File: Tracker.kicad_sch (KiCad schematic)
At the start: 10 parts, among them J1 Conn_01x04_Pin, J2 Conn_01x04, Q1 Q_NMOS_GSD, U1 LOC112P, U2 LM74700

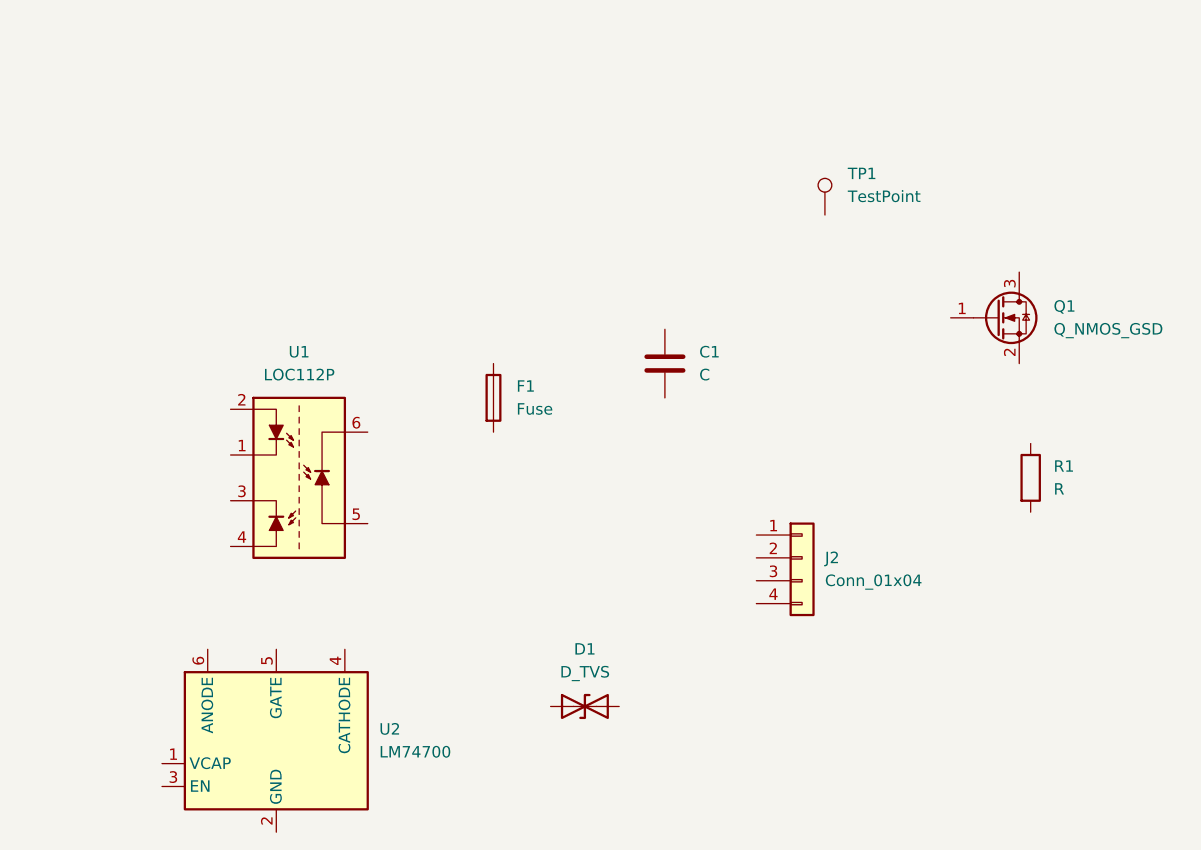
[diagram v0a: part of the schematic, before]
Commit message: Add BG95 modem sheet to Tracker
Added a new root schematic sheet for the Quectel BG95-M3 cellular module and the SIM card connector. Updated the KiCad project metadata to include the new sheet and register the associated power net and symbol references so the design is fully linked in the project.
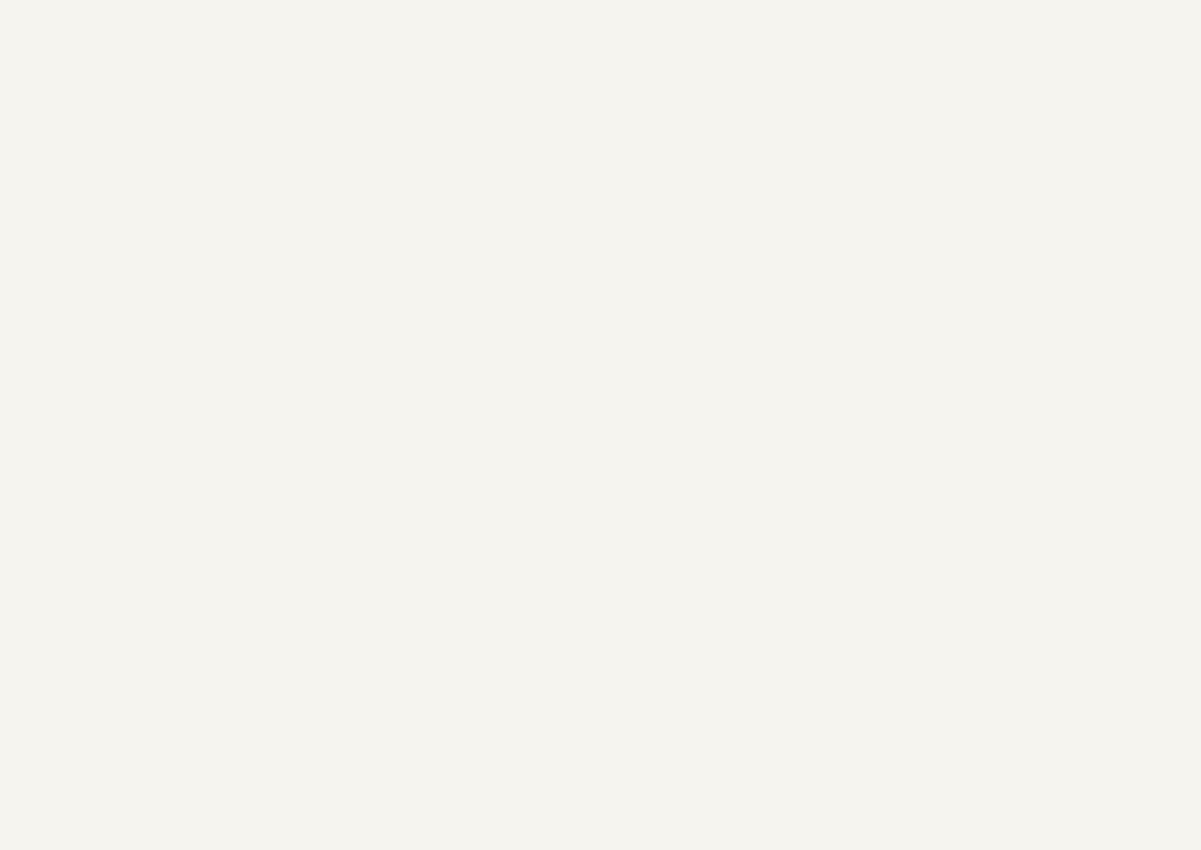
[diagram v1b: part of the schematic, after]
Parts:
- removed C1: C, symbol Device:C
- removed D1: D_TVS, symbol Device:D_TVS
- removed F1: Fuse, Package_QFP:PQFP-160_28x28mm_P0.65mm, symbol Device:Fuse
- removed J2: Conn_01x04, Package_TO_SOT_SMD:SOT-23-6, symbol Connector_Generic:Conn_01x04
- removed Q1: Q_NMOS_GSD, Package_QFP:TQFP-44_10x10mm_P0.8mm, symbol Transistor_FET:Q_NMOS_GSD
- removed R1: R, symbol Device:R
- removed TP1: TestPoint, Package_QFP:TQFP-44_10x10mm_P0.8mm, symbol Connector:TestPoint
- removed U1: LOC112P, Package_DIP:IXYS_Flatpak-8_6.3x9.7mm_P2.54mm, symbol Isolator_Analog:LOC112P
- removed U2: LM74700, Package_TO_SOT_SMD:SOT-23-6, symbol Power_Management:LM74700

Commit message: Update BG95 schematic and power nets
This commit revises the tracker schematic to match the updated BG95 and power-distribution design. It adds missing power flags and net labels, updates component references and footprints, adds coaxial and connector symbols, and swaps several passives/ferrite beads to better reflect the final BOM. The netlist is also cleaned up by renaming references and correcting no-connect/power pin assignments so the KiCad project remains consistent and ERC-friendly.
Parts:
- removed J1: Conn_01x04_Pin, Package_DIP:IXYS_Flatpak-8_6.3x9.7mm_P2.54mm, symbol Connector:Conn_01x04_Pin
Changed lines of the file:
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@@
 	(generator_version "10.0")
 	(paper "A1")
-	(symbol
-		(lib_id "Connector:Conn_01x04_Pin")
-		(at -1282.7 -607.06 0)
-		(unit 1)
-		(body_style 1)
-		(exclude_from_sim no)
-		(in_bom yes)
-		(on_board yes)
-		(in_pos_files yes)
-		(dnp no)
-		(fields_autoplaced yes)
-		(property "Reference" "J1"
-			(at -1282.065 -613.41 0)
-			(show_name no)
-			(do_not_autoplace no)
-			(effects
-				(font
-					(size 1.27 1.27)
-				)
-			)
-		)
-		(property "Value" "Conn_01x04_Pin"
-			(at -1282.065 -610.87 0)
-			(show_name no)
-			(do_not_autoplace no)
-			(effects
-				(font
-					(size 1.27 1.27)
-				)
-			)
-		)
-		(property "Footprint" "Package_DIP:IXYS_Flatpak-8_6.3x9.7mm_P2.54mm"
-			(at -1282.7 -607.06 0)
-			(hide yes)
-			(show_name no)
-			(do_not_autoplace no)
-			(effects
-				(font
-					(size 1.27 1.27)
-				)
-			)
-		)
-		(property "Datasheet" ""
-			(at -1282.7 -607.06 0)
-			(hide yes)
-			(show_name no)
-			(do_not_autoplace no)
-			(effects
-				(font
-					(size 1.27 1.27)
-				)
-			)
-		)
-		(property "Description" "Generic connector, single row, 01x04, script generated"
-			(at -1282.7 -607.06 0)
-			(hide yes)
-			(show_name no)
-			(do_not_autoplace no)
-			(effects
-				(font
-					(size 1.27 1.27)
-				)
-			)
-		)
-		(pin "4"
-		)
-		(pin "3"
-		)
-		(pin "1"
-		)
-		(pin "2"
-		)
-		(instances
-			(project "Tracker"
-				(path "/586d1ea1-b017-4713-987c-545d658f6cc8"
-					(reference "J1")
-					(unit 1)
-				)
-			)
-		)
-	)
 	(sheet_instances
 		(path "/"

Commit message: Add GNSS and power protection
This update expands the Tracker schematic with vehicle input protection, GNSS receiver connectivity, and additional power/measurement components. It also refreshes KiCad symbol metadata and designator assignments, and renames the page-2 connector reference from J2 to J901 to match the updated schematic and BOM.
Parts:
- added C1, C3, C4: 22nF 100V, Package_SO:SOIC-8_3.9x4.9mm_P1.27mm, symbol Device:C
- added C2: C, Package_SO:SOIC-8_3.9x4.9mm_P1.27mm, symbol Device:C
- added C2: 100nF 25V, Package_SO:SOIC-8_3.9x4.9mm_P1.27mm, symbol Device:C
- added C321: 10uF, Package_SO:SOIC-8_3.9x4.9mm_P1.27mm, symbol Device:C
- added C322: 100uF, Package_SO:SOIC-8_3.9x4.9mm_P1.27mm, symbol Device:C
- added C323: 100nF, Package_SO:SOIC-8_3.9x4.9mm_P1.27mm, symbol Device:C
- added C5: 10nF, Package_SO:SOIC-8_3.9x4.9mm_P1.27mm, symbol Device:C
- added D3: SMBJ33CA, DIONM5436X244N, symbol SamacSys_Parts:SMBJ33CA
- added F1: Fuse, symbol Device:Fuse
- added IC1, IC2: BQ25601DRTWR, QFN50P400X400X80-25N-D, symbol SamacSys_Parts:BQ25601DRTWR
- added J1: Vehicle 12V 2X2, Package_TO_SOT_SMD:SOT-23, symbol Project_Parts:Vehicle 12V 2X2
- added J303: Conn_Coaxial, Package_DFN_QFN:WDFN-10-1EP_3x3mm_P0.5mm_EP1.8x2.5mm, symbol Connector:Conn_Coaxial
- added L301: 27nH, Relay_THT:Relay_DPDT_Finder_30.22, symbol Device:L
- added Q2, Q4: 2N7002, Package_TO_SOT_SMD:SOT-23, symbol Transistor_FET:2N7002
- added Q3: DMT6007LFGQ-7, DMTH8008LFGQ7, symbol SamacSys_Parts:DMT6007LFGQ-7
- added R3: 100k, symbol Device:R
- added R313, R314, R316, R317, R318: 10R, symbol Device:R
- added R4: 22k, symbol Device:R
- added TP1: TP 1, DMTH8008LFGQ7, symbol Connector:TestPoint
- added TP309: TP 309, RF_GPS:ublox_MAX, symbol Connector:TestPoint
- added TP310: TP 310, RF_GPS:ublox_MAX, symbol Connector:TestPoint
- added TP311: TP 311, RF_GPS:ublox_MAX, symbol Connector:TestPoint
- added U1: LM74700, Package_TO_SOT_SMD:SOT-23-6, symbol Power_Management:LM74700
- added U305: MAX-M10S, RF_GPS:ublox_MAX, symbol RF_GPS:MAX-M10S
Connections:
- new net: C5.1, Q2.1 (G), R3.1, R4.2
- new net: C1.1, C2.1, D3.2, F1.2, Q3.1 (S_1), Q3.2 (S_2), Q3.3 (S_3), U1.3 (EN), U1.6 (ANODE)
- new net: Q3.4 (G), U1.5 (GATE)
- new net: TP311.1, U305.18 (~{SAFEBOOT})
- new net: C2.2, U1.1 (VCAP)
- new net: J303.1 (In), L301.1, U305.14 (VCC_RF)
- new net: L301.2, R313.2
- new net: F1.1, J1.1 (Batery_12V)
- new net: R313.1, U305.11 (RF_IN)
- new net: TP309.1, U305.4 (TIMEPULSE)
- new net: TP310.1, U305.9 (~{RESET})
- new net 3V3_AON: C323.1, R316.2, U305.6 (V_BCKP)
- new net 3V3_AUX: C321.1, C322.1, U305.7 (VCC_IO), U305.8 (VCC)
- new net GND: C1.2, C3.2, C321.2, C322.2, C323.2, C4.2, C5.2, D3.1, J1.2 (GND), J303.2 (Ext), Q2.2 (S), R314.1, R317.1, R4.1, U1.2 (GND), U305.1 (GND), U305.10 (GND), U305.12 (GND)
- new net GNSS_UART_RX: U305.2 (TXD)
- new net GNSS_UART_TX: U305.3 (RXD)
- new net IGN_IN: J1.3 (Ignition), R3.2
- new net IGN_WAKE_N: Q2.3 (D), R316.1
- new net VIN_PROT: C3.1, Q3.5 (D_1), R318.2, TP1.1, U1.4 (CATHODE)
- new net VIN_SENSE: C4.1, R317.2, R318.1
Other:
- note added: "GNSS RECEIVER"
- note added: "VEHICLE INPUT"

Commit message: More adjustment
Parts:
- removed C2: C, Package_SO:SOIC-8_3.9x4.9mm_P1.27mm, symbol Device:C
- removed IC2: BQ25601DRTWR, QFN50P400X400X80-25N-D, symbol SamacSys_Parts:BQ25601DRTWR
- removed R314: 10R, symbol Device:R
- added C10, C11: 47uF 100V, Package_SO:SOIC-8_3.9x4.9mm_P1.27mm, symbol Device:C
- added C12: 470nF 16V, Package_SO:SOIC-8_3.9x4.9mm_P1.27mm, symbol Device:C
- added C13: 2.2uF 10V, Package_SO:SOIC-8_3.9x4.9mm_P1.27mm, symbol Device:C
- added C14: 1uF 10V, Package_SO:SOIC-8_3.9x4.9mm_P1.27mm, symbol Device:C
- added C15: 120pF C0G, Package_SO:SOIC-8_3.9x4.9mm_P1.27mm, symbol Device:C
- added C16, C17, C18: 47uF 10V, Package_SO:SOIC-8_3.9x4.9mm_P1.27mm, symbol Device:C
- added C23: 1uF 25V, Package_SO:SOIC-8_3.9x4.9mm_P1.27mm, symbol Device:C
- added C24: 10uF 25V, Package_SO:SOIC-8_3.9x4.9mm_P1.27mm, symbol Device:C
- added C26, C28, C30, C32: 10uF 10V, Package_SO:SOIC-8_3.9x4.9mm_P1.27mm, symbol Device:C
- added C29: 4.7uF 10V, Package_SO:SOIC-8_3.9x4.9mm_P1.27mm, symbol Device:C
- added C6, C7: 2.2uF 100V, Package_SO:SOIC-8_3.9x4.9mm_P1.27mm, symbol Device:C
- added C8, C9: 4.7uF 100V, Package_SO:SOIC-8_3.9x4.9mm_P1.27mm, symbol Device:C
- added D2: LED green, QFN50P400X400X80-25N-D, symbol Device:LED
- added L1: 1uH Isat >=4A, Relay_THT:Relay_DPDT_Finder_30.22, symbol Device:L
- added L3: 1uH Isat >=3.5A, Relay_THT:Relay_DPDT_Finder_30.22, symbol Device:L
- added R10: 402k 1%, symbol Device:R
- added R11, R7, R8: 100k 1%, symbol Device:R
- added R23: 30.9k 1%, symbol Device:R
- added R26, R27: 100k, symbol Device:R
- added R28: 20m 1% 1W, symbol Device:R
- added R321, R322, R323: 10R, symbol Device:R
- added R6: 4.7R, symbol Device:R
- added R9: 24.9k 1%, symbol Device:R
- added TH1: 10k NTC, Resistor_THT:R_Array_SIP4, symbol Device:Thermistor_NTC
- added TP4: (no value), Relay_THT:Relay_DPDT_Schrack-RT2-FormC_RM5mm, symbol Connector:TestPoint
- added TP5: TP 5, Relay_THT:Relay_DPDT_Schrack-RT2-FormC_RM5mm, symbol Connector:TestPoint
- added TP6: TP 6, Relay_THT:Relay_DPDT_Schrack-RT2-FormC_RM5mm, symbol Connector:TestPoint
- added U2: LM76003QRNPRQ1, LM76003QRNPRQ1, symbol SamacSys_Parts:LM76003QRNPRQ1
- renumbered IC1 to U5
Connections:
- net GND: now also Q4.2 (S), U5.17 (GND_1), U5.18 (GND_2), U5.25 (EP), C10.1, C11.1, C13.1, C14.2, C16.1, C17.1, C18.1, C23.2, C24.1, C26.2, C28.2, C29.2, C32.2, C6.1, C7.1, C8.1, C9.1, R11.1, R23.1, R27.1, R7.1, R9.1, TH1.2, U2.13 (AGND_1), U2.14 (AGND_2), U2.15 (AGND_3), U2.17 (SYNC/MODE), U2.19 (NC_2), U2.23 (NC_3), U2.24 (PGND_1), U2.25 (PGND_2), U2.26 (PGND_3), U2.27 (NC_4), U2.28 (NC_5), U2.29 (NC_6), U2.30 (NC_7), U2.31 (EP), U2.7 (NC_1)
- net VIN_PROT: now also C6.2, C7.2, L1.1
- net VBUS_CHG: now reaches U5.1 (VBUS)
- net VBUS_CHG: now also U5.24 (VAC), C23.1
- net at U5.11 (TS): now also R23.2, R321.2, TH1.1
- net at U5.12 (~{QON}): now also TP4.1
- net BAT_CHG: now reaches U5.13 (BAT_1)
- net BAT_CHG: now also U5.14 (BAT_2), C28.1, R323.2
- net SYS_CHG: now reaches U5.15 (SYS_1)
- net SYS_CHG: now also U5.16 (SYS_2), C26.1, C32.1, L3.2, R28.2
- net at U5.19 (SW_1): now also U5.20 (SW_2), C30.1, L3.1
- net at U5.21 (BTST): now also C30.2
- net REGN: now reaches U5.22 (REGN)
- net REGN: now also Q4.3 (D), C29.1, R26.2, R321.1, R322.1
- net at U5.23 (PMID): now also C24.2
- net at U5.4 (STAT): now also D2.1 (K)
- net I2C_SCL: now reaches U5.5 (SCL)
- net I2C_SDA: now reaches U5.6 (SDA)
- net CHG_INT_N: now reaches U5.7 (~{INT})
- net at U5.9 (~{CE}): now also R26.1
- net CHG_EN: now reaches Q4.1 (G)
- net CHG_EN: now also R27.2
- new net: C14.1, R6.2, U2.9 (BIAS)
- new net: D2.2 (A), R322.2
- new net: C15.1, R8.2, R9.2, U2.12 (FB)
- new net: R7.2, U2.10 (RT)
- new net: R10.1, R11.2, U2.18 (EN)
- new net: C10.2, C11.2, C8.2, C9.2, L1.2, R10.2, U2.20 (PVIN_1), U2.21 (PVIN_2), U2.22 (PVIN_3)
- new net: C12.1, U2.6 (BOOT)
- new net: C13.2, U2.8 (VCC)
- new net 5V_VEH: C12.2, C15.2, C16.2, C17.2, C18.2, R6.1, R8.1, U2.1 (SW_1), U2.2 (SW_2), U2.3 (SW_3), U2.4 (SW_4), U2.5 (SW_5)
- new net BAT_CELL: R323.1, TP6.1
- new net BUCK_PG: U2.16 (PGOOD)
- new net VSYS: R28.1, TP5.1
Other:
- note added: "CHARGER + POWER PATH"
- moved on the sheet: Q4

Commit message: 5V source MUX
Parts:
- added C19: 100nF, symbol Device:C
- added C20, C21: 1uF 16V, symbol Device:C
- added C22: 4.7uF 16V, symbol Device:C
- added R13: 316k 1%, TPS2121RUXR, symbol Device:R
- added R14: 100k 1%, TPS2121RUXR, symbol Device:R
- added R15: 237% 1%, TPS2121RUXR, symbol Device:R
- added R16, R18: 49.9k 1%, TPS2121RUXR, symbol Device:R
- added R17: 237k 1%, TPS2121RUXR, symbol Device:R
- added R19: 30.1k 1%, TPS2121RUXR, symbol Device:R
- added R21: 20m 1% 1W, TPS2121RUXR, symbol Device:R
- added TP3: TestPoint, symbol Connector:TestPoint
- added U3: TPS2121RUXR, TPS2121RUXR, symbol SamacSys_Parts:TPS2121RUXR
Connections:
- net GND: now also C19.2, C20.2, C21.2, C22.2, R14.2, R16.2, R18.2, R19.1, U3.12 (GND), U3.3 (CP2)
- net VBUS_CHG: now also R21.2
- new net: R13.2, R14.1, U3.6 (PR1)
- new net: C22.1, R21.1, TP3.1, U3.1 (OUT_1), U3.8 (OUT_2)
- new net: R15.2, R16.1, U3.5 (OV1)
- new net: C19.1, U3.11 (SS)
- new net: R17.2, R18.1, U3.4 (OV2)
- new net: R19.2, U3.10 (ILIM)
- new net MUX_ST: U3.9 (ST)
- new net VBUS_USB: C21.1, R17.1, U3.2 (IN2)
- new net VCC: C20.1, R13.1, R15.1, U3.7 (IN1)
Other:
- note added: "5V SOURCE MUX"
- note added: "INPUT FILTER + AUTOMOTIVE BUCK"

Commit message: power
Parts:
- added BT1: BHC-18650-1P, BHC186501P, symbol SamacSys_Parts:BHC-18650-1P
- added C30, C31, C32: 100nF, QFN65P400X400X100-17N-D, symbol Device:C
- added Q1, Q5: CSD16406Q3, DQG_VSON-CLIP, symbol SamacSys_Parts:CSD16406Q3
- added R31: 2.2k, symbol Device:R
- added R32, R33: 5.2M, symbol Device:R
- added TP12: TP 12, symbol Connector:TestPoint
- added TP13: TP 13, symbol Connector:TestPoint
- added U4: INA3221AIRGVR, QFN65P400X400X100-17N-D, symbol SamacSys_Parts:INA3221AIRGVR
- added U6: BQ29700DSER, SON50P150X150X80-6N, symbol SamacSys_Parts:BQ29700DSER
- added U7: TPS3840DL35DBVR, SOT95P280X145-5N, symbol SamacSys_Parts:TPS3840DL35DBVR
- C25: renamed from C30; value 10uF 10V -> 47Nf 16v
- renumbered C32 to C27
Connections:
- net 3V3_AON: now also C30.1, U4.16 (VPU), U4.4 (VS)
- net BAT_CELL: now also BT1.1 (-), C31.1, U4.1 (IN-3), U6.5 (BAT)
- net BAT_CHG: now also U4.2 (IN+3)
- net GND: now also C30.2, C32.2, Q5.1 (S_1), Q5.2 (S_2), Q5.3 (S_3), R31.1, R33.2, TP12.1, TP13.1, U4.17 (GND_2), U4.3 (GND_1), U4.5 (A0), U7.3 (GND)
- net I2C_SDA: now also U4.7 (SDA)
- net SYS_CHG: now also U4.15 (IN+2)
- net VBUS_CHG: now also U4.11 (IN-1)
- net VSYS: now also C32.1, U4.14 (IN-2), U7.2 (VDD), U7.4 (~{MR}/NC)
- new net: Q5.4 (G), R33.1, U6.3 (DOUT)
- new net: BT1.2 (+), C31.2, Q1.1 (S_1), Q1.2 (S_2), Q1.3 (S_3), R32.2, U6.4 (VSS)
- new net: Q1.4 (G), R32.1, U6.2 (COUT)
- new net: R31.2, U6.6 (V-)
- new net: Q1.5 (D_1), Q5.5 (D_1)
- new net ICC_SCL: U4.6 (SCL)
- new net PM_ALERT_N: U4.8 (WARNING), U4.9 (CRITICAL)
- new net SYS_LOW_N: U7.1 (~{RESET})
- new net VBUS_MUX: U4.12 (IN+1)
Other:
- note added: "BACKUP CELL"
- note added: "POWER MONITORING"

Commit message: dec
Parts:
- removed TP12: TP 12, symbol Connector:TestPoint
- removed TP13: TP 13, symbol Connector:TestPoint
- added C33, C37, C38, C46, C47: 10uF 10V, QFN65P400X400X100-17N-D, symbol Device:C
- added C34, C35, C39, C40, C41: 22uF 10V, QFN65P400X400X100-17N-D, symbol Device:C
- added C36: 220uF 6.3V polymer, QFN65P400X400X100-17N-D, symbol Device:C_Polarized
- added C42: 100nF, QFN65P400X400X100-17N-D, symbol Device:C
- added C43, C45: 4.7uF 10V, QFN65P400X400X100-17N-D, symbol Device:C
- added CSC1: 1F 2.7V, QFN65P400X400X100-17N-D, symbol Device:C_Polarized
- added L4: 0.47uH 5.4A, Relay_THT:Relay_DPDT_Finder_30.22, symbol Device:L
- added L5: 2.2uH 4.4A, Relay_THT:Relay_DPDT_Finder_30.22, symbol Device:L
- added L7, L8: 2.2uH, Relay_THT:Relay_DPDT_Finder_30.22, symbol Device:L
- added R29: 6.65k 1%, symbol Device:R
- added R35, R36: R, TPS2121RUXR, symbol Device:R
- added R37: 100k, TPS2121RUXR, symbol Device:R
- added R39: 4.75k 1%, symbol Device:R
- added R40: 22.1k 1%, symbol Device:R
- added R42, R43: 1M 1%, symbol Device:R
- added R44, R45: 267k 1%, symbol Device:R
- added R46: 100k, symbol Device:R
- added TP10, TP11, TP9: TP 9, symbol Connector:TestPoint
- added TP208: TP 208, symbol Connector:TestPoint
- added U10, U11: TPS62840DLCR, SON50P150X200X100-8N-D, symbol SamacSys_Parts:TPS62840DLCR
- added U8: TPS63802DLAR, TPS63802DLAR, symbol SamacSys_Parts:TPS63802DLAR
- added U9: TPS61094DSSR, SON50P200X300X80-13N-D, symbol SamacSys_Parts:TPS61094DSSR
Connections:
- net ICC_SCL is gone; now on net I2C_SCL: U4.6 (SCL)
- net 3V3_AON: now also C47.1, L8.2, TP10.1, U10.7 (SW)
- net 3V3_AUX: now also C46.1, L7.2, TP11.1, U11.8 (VOS)
- net GND: now also C33.2, C34.2, C35.2, C36.2, C37.2, C38.2, C39.2, C40.2, C41.2, C42.2, C43.2, C45.2, C46.2, C47.2, CSC1.2, R29.1, R36.2, R37.2, R39.1, R40.1, R43.1, R44.2, R45.2, R46.2, U10.1 (GND), U10.3 (MODE), U10.6 (STOP), U11.1 (GND), U11.3 (MODE), U11.6 (STOP), U8.2 (MODE), U8.3 (AGND), U8.8 (GND), U9.13 (EP), U9.7 (PGND), U9.8 (AGND)
- net VBAT_BG95: now also C34.1, C35.1, C36.1, R35.1, U8.6 (VOUT)
- net VSYS: now also C33.1, C37.1, C45.1, U11.2 (VIN), U8.10 (VIN), U9.2 (MODE), U9.3 (EN), U9.4 (VIN)
- new net: R44.1, U10.5 (VSET)
- new net: L8.1, U10.8 (VOS)
- new net: R45.1, U11.5 (VSET)
- new net: L7.1, U11.7 (SW)
- new net: R29.2, U9.12 (VCHG)
- new net: L4.1, U8.9 (L1)
- new net: L4.2, U8.7 (L2)
- new net: L5.1, U9.5 (SW)
- new net: C38.1, CSC1.1, L5.2, R42.2, U9.6 (SUP)
- new net: R39.2, U9.1 (OSEL)
- new net: R40.2, U9.11 (ICHG)
- new net: TP208.1, U8.5 (PG)
- new net: R35.2, R36.1, U8.4 (FB)
- new net AUX_EN: R46.1, U11.4 (EN)
- new net BG95_PWR_EN: R37.1, U8.1 (EN)
- new net VOUT_SC: C39.1, C40.1, C41.1, C43.1, TP9.1, U10.2 (VIN), U10.4 (EN), U9.10 (VOUT_2), U9.9 (VOUT_1)
- new net VSUP_SENSE: C42.1, R42.1, R43.2
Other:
- note added: "3.3V RAIL"
- note added: "BG95-M3 SUPPLY"
- note added: "LAST-GASP"
- moved on the sheet: BT1, C1, C10, C11, C12, C13, C14, C15, C16, C17, C18, C19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

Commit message: hierarchy
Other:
- added sheet CELLULAR (cellular.kicad_sch)
- added sheet MCU_PERIPHERALS (mcu_peripherals.kicad_sch)
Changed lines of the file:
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@@
+		)
+	)
+	(sheet
+		(at 50.8 0)
+		(size 44.45 3.81)
+		(exclude_from_sim no)
+		(in_bom yes)
+		(on_board yes)
+		(dnp no)
+		(fields_autoplaced yes)
+		(stroke
+			(width 0.1524)
+			(type solid)
+		)
+		(fill
+			(color 0 0 0 0)
+		)
+		(property "Sheetname" "CELLULAR"
+			(at 50.8 -0.7116 0)
+			(show_name no)
+			(do_not_autoplace no)
+			(effects
+				(font
+					(size 1.27 1.27)
+				)
+				(justify left bottom)
+			)
+		)
+		(property "Sheetfile" "cellular.kicad_sch"
+			(at 50.8 4.3946 0)
+			(show_name no)
+			(do_not_autoplace no)
+			(effects
+				(font
+					(size 1.27 1.27)
+				)
+				(justify left top)
+			)
+		)
+		(instances
+			(project "Tracker"
+				(path "/586d1ea1-b017-4713-987c-545d658f6cc8"
+					(page "3")
+				)
+			)
+		)
+	)
+	(sheet
+		(at 0 0)
+		(size 50.8 3.81)
+		(exclude_from_sim no)
+		(in_bom yes)
+		(on_board yes)
+		(dnp no)
+		(fields_autoplaced yes)
+		(stroke
+			(width 0.1524)
+			(type solid)
+		)
+		(fill
+			(color 0 0 0 0)
+		)
+		(property "Sheetname" "MCU_PERIPHERALS"
+			(at 0 -0.7116 0)
+			(show_name no)
+			(do_not_autoplace no)
+			(effects
+				(font
+					(size 1.27 1.27)
+				)
+				(justify left bottom)
+			)
+		)
+		(property "Sheetfile" "mcu_peripherals.kicad_sch"
+			(at 0 4.3946 0)
+			(show_name no)
+			(do_not_autoplace no)
+			(effects
+				(font
+					(size 1.27 1.27)
+				)
+				(justify left top)
+			)
+		)
+		(instances
+			(project "Tracker"
+				(path "/586d1ea1-b017-4713-987c-545d658f6cc8"
+					(page "2")
+				)
+			)
 		)
 	)
